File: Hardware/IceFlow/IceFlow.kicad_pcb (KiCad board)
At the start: 2 copper layers, 84 x 52.5 mm, 22 parts, among them J1 Barrel_Jack_Switch, J2 Conn_01x04, J3 TFT_Display_wTouch, J4 Conn_02x02_Odd_Even, J6 Conn_02x05_Odd_Even, J8 Power_Sw, U1 NCP1117-3.3_SOT223, U2 ESP32-WROVER-E

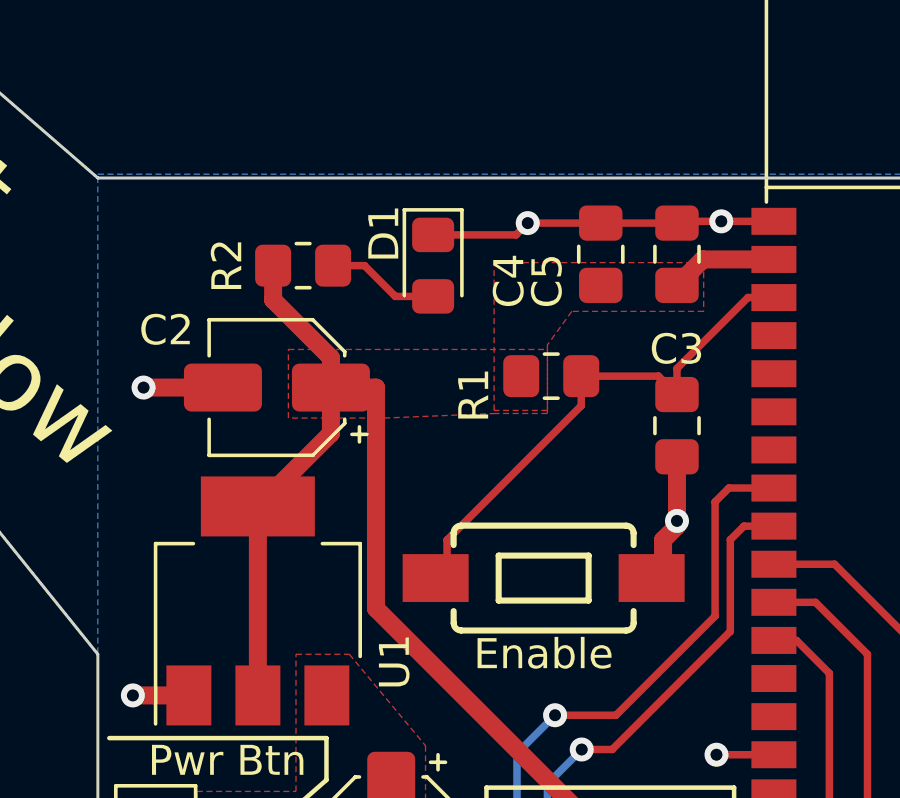
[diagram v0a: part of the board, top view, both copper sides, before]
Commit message: Pin map changes
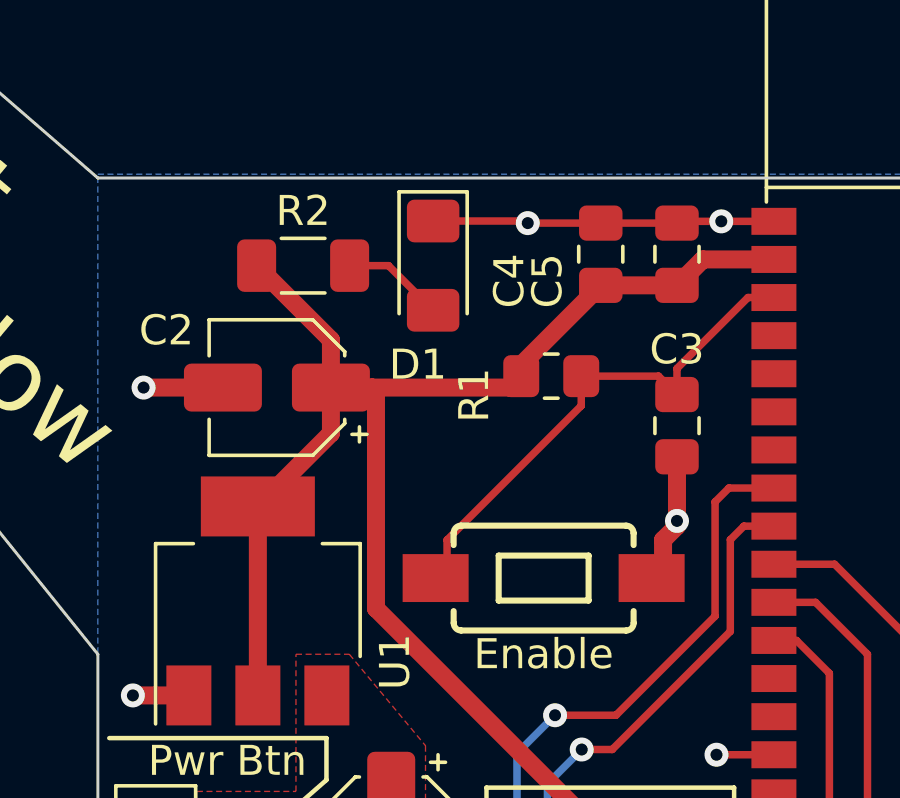
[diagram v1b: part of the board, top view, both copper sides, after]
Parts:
- D1: footprint LED_SMD:LED_0805_2012Metric_Pad1.15x1.40mm_HandSolder -> LED_SMD:LED_1206_3216Metric_Pad1.42x1.75mm_HandSolder
- R2: footprint Resistor_SMD:R_0805_2012Metric_Pad1.20x1.40mm_HandSolder -> Resistor_SMD:R_1206_3216Metric_Pad1.30x1.75mm_HandSolder
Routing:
- net +3V3: track 105.7 -> 117.7 mm
- removed copper zone on F.Cu, net +3V3
